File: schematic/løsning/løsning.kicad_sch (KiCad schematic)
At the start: 5 parts, among them U1 LM2575-5.0BT

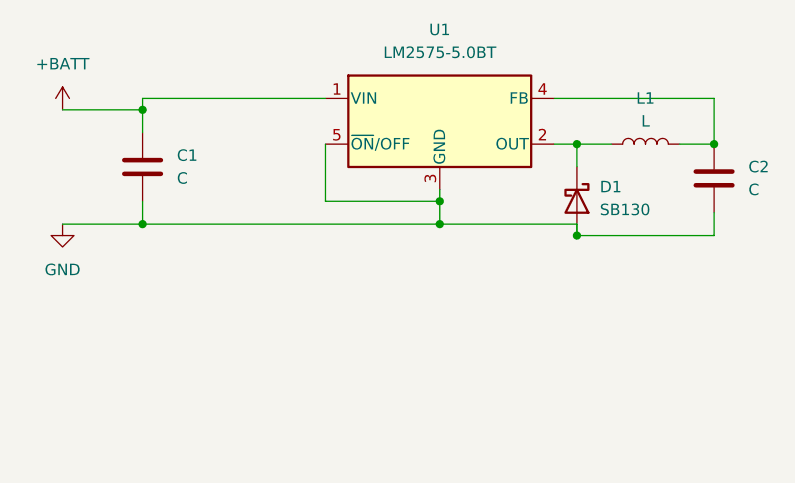
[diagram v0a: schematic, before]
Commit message: started adding voltage divider
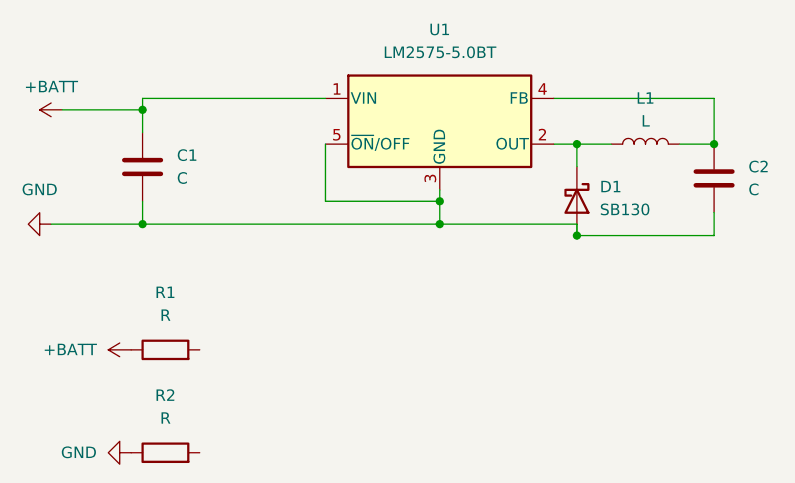
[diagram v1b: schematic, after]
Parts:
- added R1, R2: R, symbol Device:R
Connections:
- net +BATT: now also R1.1
- net GND: now also R2.1
